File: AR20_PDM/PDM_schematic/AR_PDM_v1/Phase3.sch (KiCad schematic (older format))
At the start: 12 parts, among them Q3 BTS50025-1TAD, U6 INA233

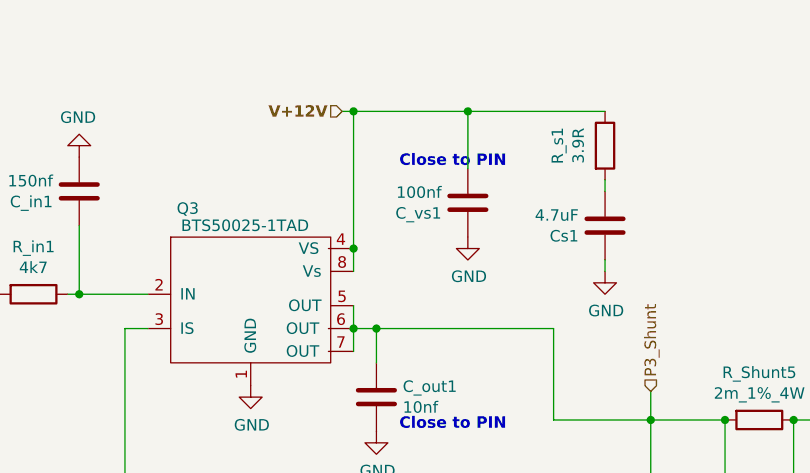
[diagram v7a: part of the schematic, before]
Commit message: First Complete Draft of PCB and schematics, - minus see discription
- missing correct smd switch header
- missing correct main power plug
- tweeks still needs to be done
- Extra inspection of schematics pending
- proper, in depth quiality controll of pcb work pending
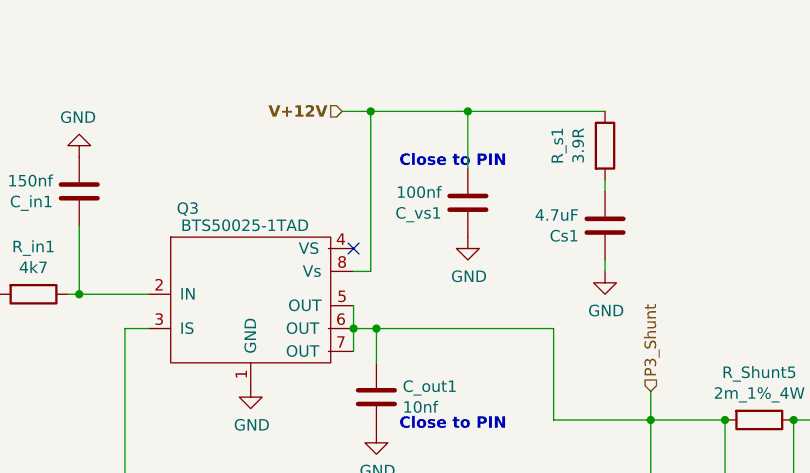
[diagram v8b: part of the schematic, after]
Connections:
- net V+12V: no longer Q3.4 (VS)
- no-connect marks 0 -> 1
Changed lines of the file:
@@
 $Descr A4 11693 8268
 encoding utf-8
-Sheet 4 13
+Sheet 3 13
 Title ""
 Date ""
@@
 P3_SDA
 Wire Wire Line
-	4650 1600 4700 1600
-Wire Wire Line
-	4700 2300 4700 2200
-Wire Wire Line
-	4700 2200 4700 1600
-Connection ~ 4700 2200
-Connection ~ 4700 1600
-Wire Wire Line
-	4700 1600 5200 1600
-Wire Wire Line
 	4700 2550 4700 2650
 Connection ~ 4700 2550
@@
 Wire Wire Line
 	3700 2550 3700 3300
+Wire Wire Line
+	4650 1600 4775 1600
+Wire Wire Line
+	4775 2300 4700 2300
+Wire Wire Line
+	4775 1600 4775 2300
+NoConn ~ 4700 2200
+Connection ~ 4775 1600
+Wire Wire Line
+	4775 1600 5200 1600
 $EndSCHEMATC
